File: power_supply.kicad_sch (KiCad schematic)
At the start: 46 parts, among them J3 JST_SH_1x4_SM04B-SRSS-TB-LF-SN, Q2 DMG1012T-7, U8 MPM54304GMN-0001, U9 LT3033EUDC_QFN

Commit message: [#52835] update project name
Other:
- title: LPDDR5 SO-DIMM -> LPDDR5 Testbed
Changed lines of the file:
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@@
   (paper "A3")
   (title_block
-    (title "LPDDR5 SO-DIMM")
+    (title "LPDDR5 Testbed")
     (date "2023-12-19")
     (rev "1.0.0")

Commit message: [#52835] schematics: update dc/dc symbol from lib
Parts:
- U8: footprint antmicro-footprints:MPS_LGA-33 -> antmicro-footprints:LGA-33_7x7mm_P0.65mm
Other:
- moved on the sheet: U8
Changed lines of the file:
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@@
     (stroke (width 0) (type default) (color 0 0 0 0))
   )
-  (polyline (pts (xy 195.58 120.65) (xy 158.115 120.65))
+  (polyline (pts (xy 184.785 123.825) (xy 147.32 123.825))
     (stroke (width 0) (type default) (color 0 0 0 0))
   )
@@
     (stroke (width 0) (type default) (color 0 0 0 0))
   )
-  (polyline (pts (xy 158.115 111.125) (xy 195.58 111.125))
+  (polyline (pts (xy 147.32 114.3) (xy 184.785 114.3))
     (stroke (width 0) (type default) (color 0 0 0 0))
   )
@@
     (stroke (width 0) (type default) (color 0 0 0 0))
   )
+  (wire (pts (xy 193.04 114.3) (xy 194.31 114.3))
+    (stroke (width 0) (type default) (color 0 0 0 0))
+  )
   (polyline (pts (xy 229.235 53.975) (xy 229.235 55.245))
     (stroke (width 0) (type default) (color 0 0 0 0))
@@
     (stroke (width 0) (type default) (color 0 0 0 0))
   )
-  (polyline (pts (xy 158.115 111.125) (xy 158.115 120.65))
+  (polyline (pts (xy 147.32 114.3) (xy 147.32 123.825))
     (stroke (width 0) (type default) (color 0 0 0 0))
   )
@@
     (stroke (width 0) (type default) (color 0 0 0 0))
   )
-  (polyline (pts (xy 195.58 111.125) (xy 195.58 120.65))
+  (polyline (pts (xy 184.785 114.3) (xy 184.785 123.825))
     (stroke (width 0) (type default) (color 0 0 0 0))
   )
@@
     (stroke (width 0) (type default) (color 0 0 0 0))
   )
-  (wire (pts (xy 208.28 119.38) (xy 208.28 120.015))
+  (wire (pts (xy 193.04 114.3) (xy 193.04 115.57))
     (stroke (width 0) (type default) (color 0 0 0 0))
   )
@@
   )
   (text "Note: \nDefault I2C addres: 0x68\nWhen GPIO is configured as \nADD pin I2C addres changes to 0x6B"
-    (at 158.75 120.015 0)
+    (at 147.955 123.19 0)
     (effects (font (size 1.27 1.27)) (justify left bottom))
   )
@@
       (effects (font (size 1.27 1.27) (thickness 0.15)))
     )
-    (property "Footprint" "antmicro-footprints:MPS_LGA-33" (id 2) (at 241.3 86.36 0)
+    (property "Footprint" "antmicro-footprints:LGA-33_7x7mm_P0.65mm" (id 2) (at 241.3 86.36 0)
       (effects (font (size 1.27 1.27) (thickness 0.15)) (justify left bottom) hide)
     )
@@
     (pin "2")
   )
-  (symbol (lib_id "antmicropower:GND") (at 208.28 120.015 0) (unit 1)
-    (in_bom yes) (on_board yes)
-    (property "Reference" "#PWR0214" (id 0) (at 217.17 122.555 0)
-      (effects (font (size 1.27 1.27) (thickness 0.15)) (justify left bottom) hide)
-    )
-    (property "Value" "GND" (id 1) (at 208.28 123.825 0)
-      (effects (font (size 1.27 1.27) (thickness 0.15)))
-    )
-    (property "Footprint" "" (id 2) (at 217.17 127.635 0)
-      (effects (font (size 1.27 1.27) (thickness 0.15)) (justify left bottom) hide)
-    )
-    (property "Datasheet" "" (id 3) (at 217.17 132.715 0)
-      (effects (font (size 1.27 1.27) (thickness 0.15)) (justify left bottom) hide)
-    )
-    (property "Author" "Antmicro" (id 4) (at 217.17 127.635 0)
-      (effects (font (size 1.27 1.27) (thickness 0.15)) (justify left bottom) hide)
-    )
-    (property "License" "Apache-2.0" (id 5) (at 217.17 130.175 0)
-      (effects (font (size 1.27 1.27) (thickness 0.15)) (justify left bottom) hide)
-    )
+  (symbol (lib_id "antmicropower:GND") (at 193.04 115.57 0) (unit 1)
+    (in_bom yes) (on_board yes)
+    (property "Reference" "#PWR0214" (id 0) (at 201.93 118.11 0)
+      (effects (font (size 1.27 1.27) (thickness 0.15)) (justify left bottom) hide)
+    )
+    (property "Value" "GND" (id 1) (at 193.04 119.38 0)
+      (effects (font (size 1.27 1.27) (thickness 0.15)))
+    )
+    (property "Footprint" "" (id 2) (at 201.93 123.19 0)
+      (effects (font (size 1.27 1.27) (thickness 0.15)) (justify left bottom) hide)
+    )
+    (property "Datasheet" "" (id 3) (at 201.93 128.27 0)
+      (effects (font (size 1.27 1.27) (thickness 0.15)) (justify left bottom) hide)
+    )
+    (property "Author" "Antmicro" (id 4) (at 201.93 123.19 0)
+      (effects (font (size 1.27 1.27) (thickness 0.15)) (justify left bottom) hide)
+    )
+    (property "License" "Apache-2.0" (id 5) (at 201.93 125.73 0)
+      (effects (font (size 1.27 1.27) (thickness 0.15)) (justify left bottom) hide)
+    )

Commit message: Loclib
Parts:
- C10, C11: footprint antmicro-footprints:C_0805_2012Metric -> lpddr5-testbed-footprints:C_0805_2012Metric; symbol antmicroCapacitorsmisc:C_22u_25V_0805 -> lpddr5-testbed:C_22u_25V_0805
- C12: footprint antmicro-footprints:C_0402_1005Metric -> lpddr5-testbed-footprints:C_0402_1005Metric; symbol antmicroCapacitors0402:C_1u_0402 -> lpddr5-testbed:C_1u_0402
- C13: footprint antmicro-footprints:C_0402_1005Metric -> lpddr5-testbed-footprints:C_0402_1005Metric; symbol antmicroCapacitors0402:C_10n_0402 -> lpddr5-testbed:C_10n_0402
- C14, C15, C16, C17, C18, C19: footprint antmicro-footprints:C_0603_1608Metric -> lpddr5-testbed-footprints:C_0603_1608Metric; symbol antmicroCapacitors0603:C_22u_0603 -> lpddr5-testbed:C_22u_0603
- C20, C21, C8, C9: footprint antmicro-footprints:C_0402_1005Metric -> lpddr5-testbed-footprints:C_0402_1005Metric; symbol antmicroCapacitors0402:C_4u7_0402 -> lpddr5-testbed:C_4u7_0402
- D1: footprint antmicro-footprints:D_SOD-123F -> lpddr5-testbed-footprints:D_SOD-123F; symbol antmicroDiodesRectifiersSingle:PTVS48VS1UR -> lpddr5-testbed:PTVS48VS1UR
- D2: footprint antmicro-footprints:LED_0603_1608Metric_G -> lpddr5-testbed-footprints:LED_0603_1608Metric_G; symbol antmicroLEDIndicationDiscrete:LED_G_0603_KP-1608CGCK -> lpddr5-testbed:LED_G_0603_KP-1608CGCK
- J3: footprint antmicro-footprints:Conn_JST_SH_1x4_SM04B-SRSS-TB-LF-SN -> lpddr5-testbed-footprints:Conn_JST_SH_1x4_SM04B-SRSS-TB-LF-SN; symbol antmicroWire2BoardConnectors:JST_SH_1x4_SM04B-SRSS-TB-LF-SN -> lpddr5-testbed:JST_SH_1x4_SM04B-SRSS-TB-LF-SN
- POT1: footprint antmicro-footprints:Trimpot_3.8mmx3.6mm_TC33X-2-103E -> lpddr5-testbed-footprints:Trimpot_3.8mmx3.6mm_TC33X-2-103E; symbol antmicroTrimmerPotentiometers:TC33X-2-203E -> lpddr5-testbed:TC33X-2-203E
- Q2: footprint antmicro-footprints:SOT-523 -> lpddr5-testbed-footprints:SOT-523; symbol antmicroTransistorsFETsMOSFETsSingle:DMG1012T-7 -> lpddr5-testbed:DMG1012T-7
- R29, R47: footprint antmicro-footprints:R_0402_1005Metric -> lpddr5-testbed-footprints:R_0402_1005Metric; symbol antmicroResistors0402:R_0R_0402 -> lpddr5-testbed:R_0R_0402
- R30, R33, R35, R37, R39: footprint antmicro-footprints:R_0402_1005Metric -> lpddr5-testbed-footprints:R_0402_1005Metric; symbol antmicroResistors0402:R_100k_0402 -> lpddr5-testbed:R_100k_0402
- R31, R32, R41: footprint antmicro-footprints:R_0402_1005Metric -> lpddr5-testbed-footprints:R_0402_1005Metric; symbol antmicroResistors0402:R_25k5_0402 -> lpddr5-testbed:R_25k5_0402
- R34: footprint antmicro-footprints:R_0402_1005Metric -> lpddr5-testbed-footprints:R_0402_1005Metric; symbol antmicroResistors0402:R_49k9_0402 -> lpddr5-testbed:R_49k9_0402
- R36: footprint antmicro-footprints:R_0402_1005Metric -> lpddr5-testbed-footprints:R_0402_1005Metric; symbol antmicroResistors0402:R_200k_0402 -> lpddr5-testbed:R_200k_0402
- R38: footprint antmicro-footprints:R_0402_1005Metric -> lpddr5-testbed-footprints:R_0402_1005Metric; symbol antmicroResistors0402:R_130k_0402 -> lpddr5-testbed:R_130k_0402
- R40: footprint antmicro-footprints:R_0402_1005Metric -> lpddr5-testbed-footprints:R_0402_1005Metric; symbol antmicroResistors0402:R_120k_0402 -> lpddr5-testbed:R_120k_0402
- R42: footprint antmicro-footprints:R_0402_1005Metric -> lpddr5-testbed-footprints:R_0402_1005Metric; symbol antmicroResistors0402:R_1k_0402 -> lpddr5-testbed:R_1k_0402
- R43, R44, R45, R46, R52: footprint antmicro-footprints:R_0603_1608Metric -> lpddr5-testbed-footprints:R_0603_1608Metric; symbol antmicroResistors0603:R_0R_22.4A_0603 -> lpddr5-testbed:R_0R_22.4A_0603
- R50, R51: footprint antmicro-footprints:R_0402_1005Metric -> lpddr5-testbed-footprints:R_0402_1005Metric; symbol antmicroResistors0402:R_3k9_0402 -> lpddr5-testbed:R_3k9_0402
- TP1: footprint antmicro-footprints:TP_SMD_0.75mm -> lpddr5-testbed-footprints:TP_SMD_0.75mm; symbol antmicroTestPoints:TP_0.75mm_SMD -> lpddr5-testbed:TP_0.75mm_SMD
- TP2, TP3: footprint antmicro-footprints:TP_SMD_1mm -> lpddr5-testbed-footprints:TP_SMD_1mm; symbol antmicroTestPoints:TP_1mm_SMD -> lpddr5-testbed:TP_1mm_SMD
- U8: footprint antmicro-footprints:LGA-33_7x7mm_P0.65mm -> lpddr5-testbed-footprints:LGA-33_7x7mm_P0.65mm; symbol antmicroPMICVoltageRegulatorsDCDCSwitchingRegulators:MPM54304GMN-0001 -> lpddr5-testbed:MPM54304GMN-0001
- U9: footprint antmicro-footprints:QFN-20-4EP_3x4x0.75mm_P0.5mm_Layout4x6_LT3033 -> lpddr5-testbed-footprints:QFN-20-4EP_3x4x0.75mm_P0.5mm_Layout4x6_LT3033; symbol antmicroPMICVoltageRegulatorsLinear:LT3033EUDC_QFN -> lpddr5-testbed:LT3033EUDC_QFN

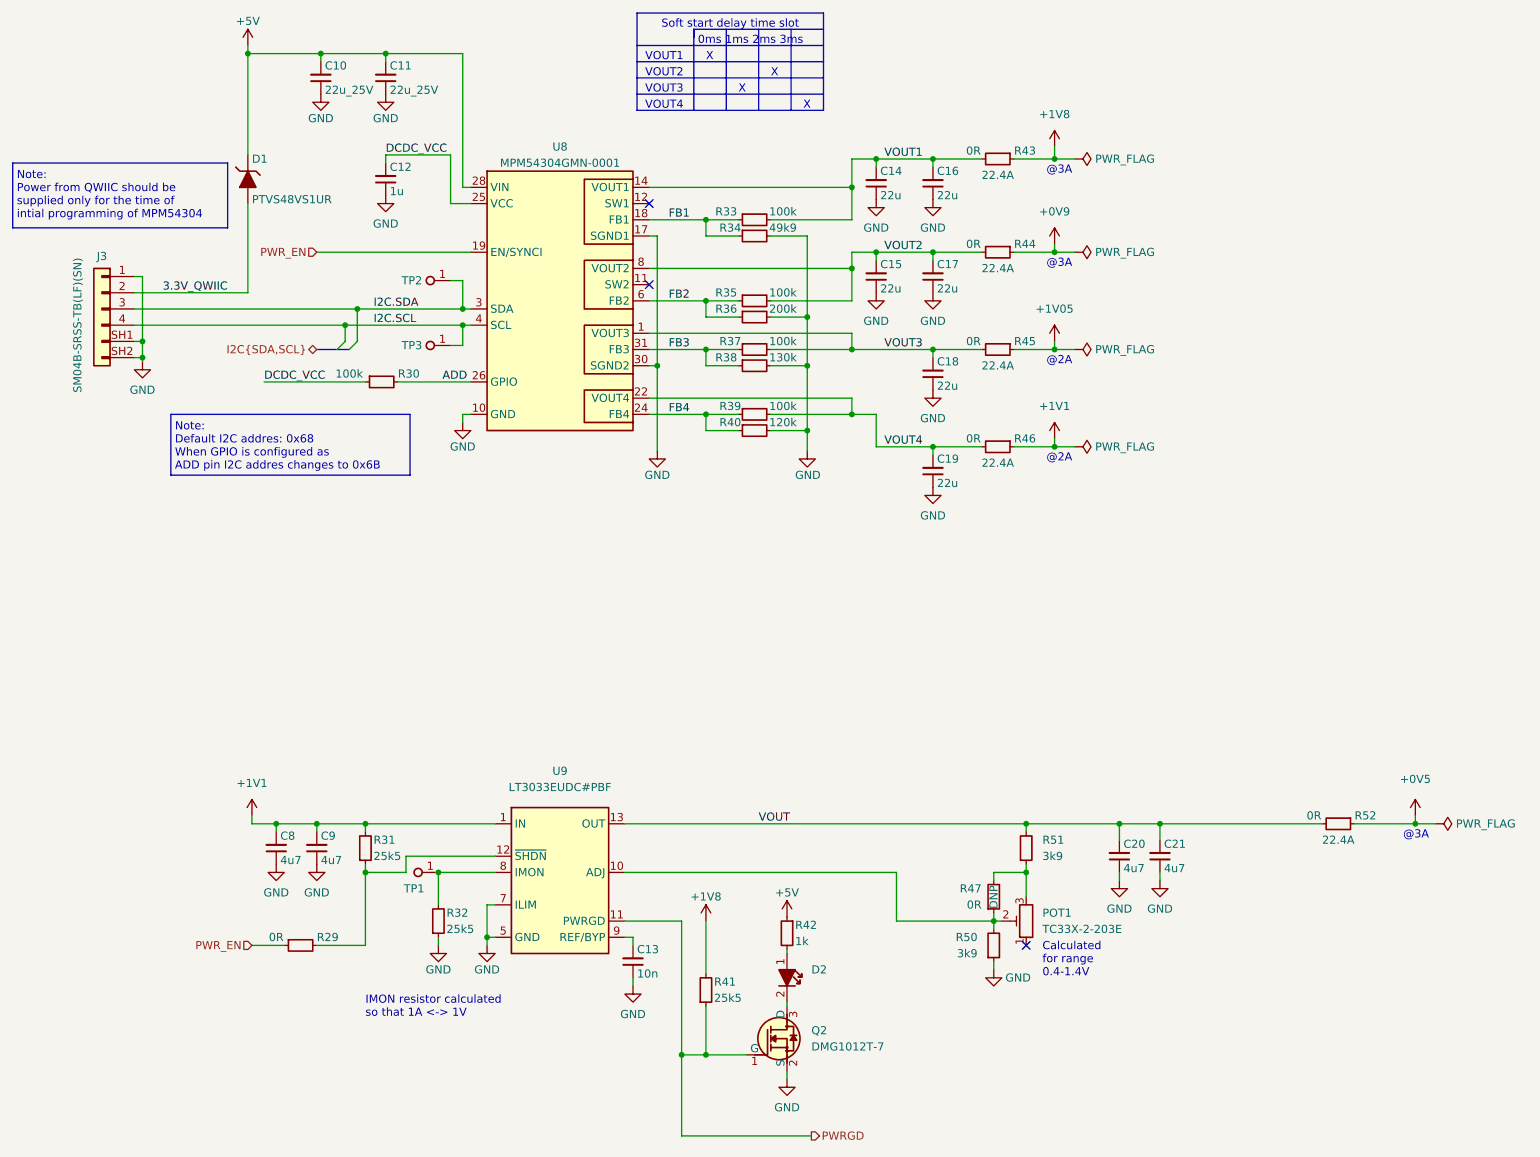
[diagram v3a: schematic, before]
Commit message: [#53267] schematic: improve power supply sequencing and power good signal
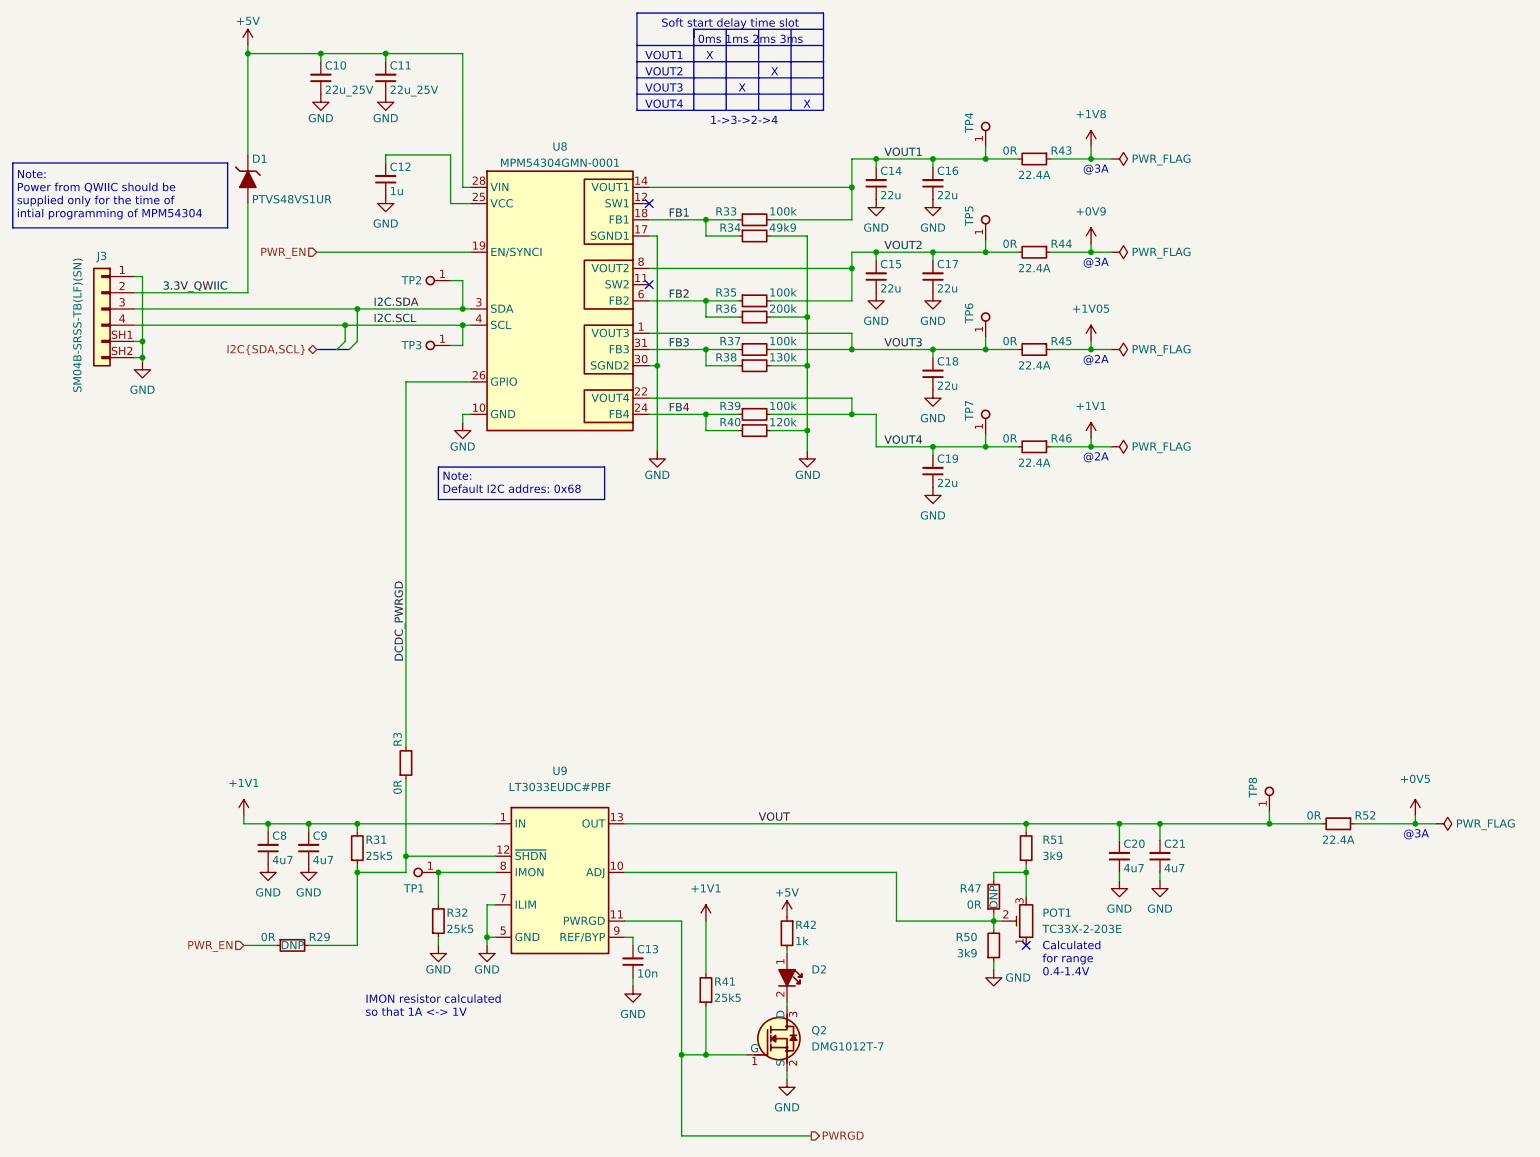
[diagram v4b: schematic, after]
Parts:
- removed R30: R_100k_0402, lpddr5-testbed-footprints:R_0402_1005Metric, symbol lpddr5-testbed:R_100k_0402
- added R3: R_0R_0402, lpddr5-testbed-footprints:R_0402_1005Metric, symbol lpddr5-testbed:R_0R_0402
- added TP4, TP5, TP6, TP7, TP8: TP_0.75mm_SMD, lpddr5-testbed-footprints:TP_SMD_0.75mm, symbol lpddr5-testbed:TP_0.75mm_SMD
- R29: DNP (none) -> DNP
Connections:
- net +1V1: now also R41.2
- net +1V8: no longer R41.2
- net VOUT: now also TP8.1
- net VOUT1: now also TP4.1
- net VOUT2: now also TP5.1
- net VOUT3: now also TP6.1
- net VOUT4: now also TP7.1
- net at R29.2, R31.1, U9.12 (~{SHDN}): now also R3.1
- net ADD renamed DCDC_PWRGD
- net DCDC_PWRGD: now also R3.2
- net DCDC_VCC: no longer names the net of C12.2, U8.25 (VCC)
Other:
- note added: "1->3->2->4"
- note added: "Note: Default I2C addres: 0x68"
- note removed: "Note: Default I2C addres: 0x68 When GPIO is configured as ADD pin I2C addres changes to 0x6B"
- moved on the sheet: C8, C9, R29, R31, R43, R44, R45, R46
